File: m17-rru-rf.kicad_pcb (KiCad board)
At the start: 4 copper layers, 255 x 165 mm, 197 parts, among them J1 13.8V, J2 Conn_Coaxial, J3 DBG_CONN, J4 SWD_CONN, J5 DA15_CONN, J6 Conn_Coaxial, Q1 BSS138, Q2 BSS138, Q3 NP100P04PDG, U1 LT1013DIDR, U10 GAT-30+, U11 CC1200, U12 AD8318, U13 AD8318, U14 STM32F405RGT6, U15 WH3538X-1, U2 LM317_SOT-223, U3 TL431, U4 RA60H3847H1, U5 TP6841, U6 TP6841, U7 CC1200, U8 GAT-30+, U9 SYBD-30-62HP+, X1 40MHz, Y1 12MHz

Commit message: TP updates, temp sensor added
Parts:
- added C90: 1u, Capacitor_SMD:C_0603_1608Metric, F.Cu at (124.7, 85.9)
- added C91: 100n, Capacitor_SMD:C_0603_1608Metric, F.Cu at (124.7, 88.4)
- added C92: 1n, Capacitor_SMD:C_0603_1608Metric, F.Cu at (124.7, 91.0)
- added FB8: Bead, Inductor_SMD:L_0603_1608Metric, F.Cu at (124.7, 98.0)
- added FB9: Bead, Inductor_SMD:L_0603_1608Metric, F.Cu at (124.7, 93.5)
- added J7: N_PAD, Connector_Coaxial:SMA_Samtec_SMA-J-P-X-ST-EM1_EdgeMount, F.Cu at (141.0, 81.3)
- added TP14: TP, TestPoint:TestPoint_Pad_D1.5mm, F.Cu at (130.0, 103.0)
- added TP15: TP, TestPoint:TestPoint_Pad_D1.5mm, F.Cu at (124.5, 103.0)
- added TP16: TP, TestPoint:TestPoint_Pad_D1.5mm, F.Cu at (130.5, 86.5)
- added TP17: TP, TestPoint:TestPoint_Pad_D1.5mm, F.Cu at (130.5, 90.0)
- C10, C17: value 100u/50V -> 100n; footprint Capacitor_SMD:CP_Elec_8x10.5 -> Capacitor_SMD:C_0603_1608Metric
- C12: value 100u/50V -> 1u; footprint Capacitor_SMD:CP_Elec_8x10.5 -> Capacitor_SMD:C_0603_1608Metric
- C13, C14: value 100n -> 100u/50V; footprint Capacitor_SMD:C_0603_1608Metric -> Capacitor_SMD:CP_Elec_8x10.5
- C18: value 22u/6.3V -> 100n
- C19: value 22u/6.3V -> 100u/50V; footprint Capacitor_SMD:C_0603_1608Metric -> Capacitor_SMD:CP_Elec_8x10.5
- C20, C21: value 47n -> 22u/6.3V
- C23, C48: value 9p1 -> 47n
- C25: value 1n5 -> 9p1
- C27, C51: value 47n -> 1n5
- C33, C56, C79: value 100n -> 47n
- C35, C82: value 10n -> 100n
- C36: value 220n -> 47n
- C37: value 39p -> 10n
- C38: value 56p -> 220n
- C39: value 2p2 -> 39p
- C40: value 10n -> 56p
- C41: value 5p1 -> 2p2
- C42: value 100p -> 10n
- C43: value 6p2 -> 5p1
- C44: value 47n -> 100p
- C45: value 47n -> 6p2
- C49: value 1n5 -> 47n
- C50: value 47n -> 9p1
- C55, C61: value 5p1 -> 47n
- C57: value 47n -> 5p1
- C58: value 5p1 -> 100n
- C60: value 10n -> 5p1
- C62: value 6p2 -> 10n
- C63: value 220n -> 5p1
- C64: value 1u -> 6p2
- C65: value 100n -> 220n
- C66: value 1n -> 1u
- C69, C72, C89: value 1n -> 100n
- C70: value 100n -> 1n
- C73, C74: value 10p -> 1n
- C75, C76: value 2u2 -> 10p
- C77, C78: value 1u -> 2u2
- C80: value 100n -> 1u
- C81: value 10n -> 1u
- C84, C85: value 100n -> 10n
- C87: value 1u -> 100n
- J1: value 13.8V -> LMT87LPM; footprint TestPoint:TestPoint_Pad_D3.0mm -> Connector_PinHeader_2.54mm:PinHeader_1x03_P2.54mm_Vertical_SMD_Pin1Left
- J2: value Conn_Coaxial -> 13.8V; footprint Connector_Coaxial:SMA_Samtec_SMA-J-P-X-ST-EM1_EdgeMount -> TestPoint:TestPoint_Pad_D3.0mm
- J3: value DBG_CONN -> N_PAD; footprint Connector_PinHeader_2.54mm:PinHeader_1x05_P2.54mm_Vertical_SMD_Pin1Left -> Connector_Coaxial:SMA_Samtec_SMA-J-P-X-ST-EM1_EdgeMount
- J4: value SWD_CONN -> DBG_CONN
- J5: value DA15_CONN -> SWD_CONN; footprint Connector_PinHeader_2.54mm:PinHeader_2x08_P2.54mm_Vertical_SMD -> Connector_PinHeader_2.54mm:PinHeader_1x05_P2.54mm_Vertical_SMD_Pin1Left
- J6: value Conn_Coaxial -> DA15_CONN; footprint Connector_Coaxial:SMA_Samtec_SMA-J-P-X-ST-EM1_EdgeMount -> Connector_PinHeader_2.54mm:PinHeader_2x08_P2.54mm_Vertical_SMD
- moved J1 241.1 mm to (89.5, 202.3)
- moved J3 226.1 mm to (322.5, 64.5), turned to 90 degrees
- moved U8 215.0 mm to (306.9, 81.2), turned to 180 degrees
- moved C87 200.8 mm to (106.0, 153.8)
- moved U6 196.9 mm to (92.7, 191.0)
- moved R21 196.9 mm to (90.0, 184.8)
- moved U14 176.5 mm to (93.7, 102.4)
- moved J2 173.6 mm to (142.0, 102.0)
- moved U13 158.9 mm to (88.3, 183.3)
- moved J6 152.5 mm to (166.8, 161.5)
- moved R22 150.9 mm to (101.4, 198.1)
- moved R40 149.1 mm to (131.2, 200.7)
- moved U7 149.1 mm to (152.9, 193.4)
- moved TP13 129.8 mm to (180.1, 161.5)
- moved C86 129.8 mm to (180.3, 166.6)
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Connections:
- C10 pad 1: /RF PA/RF_PA_VDD -> Net-(J1-Pin_1)
- C11 pad 1: /Power supply/13.8V_OUT -> /RF PA/RF_PA_VDD
- C12 pad 1: /Power supply/13.8V_OUT -> /Exciter/3.3V_IN
- C15 pad 1: Net-(U5-BST) -> /Power supply/13.8V_OUT
- C15 pad 2: Net-(U5-SW) -> GND
- C16 pad 1: Net-(U6-BST) -> /Power supply/13.8V_OUT
- C16 pad 2: Net-(U6-SW) -> GND
- C17 pad 1: /Power supply/13.8V_OUT -> Net-(U5-BST)
- C17 pad 2: GND -> Net-(U5-SW)
- C18 pad 1: GND -> Net-(U6-BST)
- C18 pad 2: /Exciter/3.3V_IN -> Net-(U6-SW)
- C19 pad 1: GND -> /Power supply/13.8V_OUT
- C19 pad 2: /Power supply/5V_OUT -> GND
- C20 pad 1: /Exciter/EXCITER_3V3 -> GND
- C20 pad 2: GND -> /Exciter/3.3V_IN
- C21 pad 1: /Exciter/EXCITER_3V3 -> GND
- C21 pad 2: GND -> /Power supply/5V_OUT
- C23 pad 1: /Exciter/40M_OUT -> /Exciter/EXCITER_3V3
- C23 pad 2: Net-(U7-EXT_XOSC) -> GND
- C25 pad 1: Net-(U7-LPF0) -> /Exciter/40M_OUT
- C25 pad 2: Net-(U7-LPF1) -> Net-(U7-EXT_XOSC)
- C27 pad 1: /Exciter/EXCITER_3V3 -> Net-(U7-LPF0)
- C27 pad 2: GND -> Net-(U7-LPF1)
- C32 pad 1: Net-(U7-DCPL_XOSC) -> /Exciter/EXCITER_3V3
- C33 pad 1: /Exciter/3.3V_IN -> /Exciter/EXCITER_3V3
- C34 pad 1: Net-(U7-DCPL_PFD_CHP) -> Net-(U7-DCPL_XOSC)
- C35 pad 1: Net-(U7-DCPL_VCO) -> /Exciter/3.3V_IN
- C36 pad 1: Net-(U7-DCPL) -> Net-(U7-DCPL_PFD_CHP)
- C37 pad 1: Net-(C37-Pad1) -> Net-(U7-DCPL_VCO)
- C37 pad 2: Net-(U7-PA) -> GND
- C38 pad 1: /Exciter/EXCITER_3V3 -> Net-(U7-DCPL)
- C38 pad 2: Net-(C38-Pad2) -> GND
- C39 pad 2: Net-(C37-Pad1) -> Net-(U7-PA)
- C40 pad 2: GND -> Net-(C40-Pad2)
- C41 pad 1: Net-(C39-Pad1) -> Net-(C41-Pad1)
- C41 pad 2: GND -> Net-(C39-Pad1)
- C43 pad 1: Net-(C43-Pad1) -> Net-(C41-Pad1)
- C44 pad 1: /Receiver/RX_3V3 -> /Exciter/EXCITER_3V3
- C45 pad 1: /Receiver/RX_3V3 -> Net-(C45-Pad1)
- C48 pad 1: Net-(U11-EXT_XOSC) -> /Receiver/RX_3V3
- C48 pad 2: /Exciter/40M_OUT -> GND
- C49 pad 1: Net-(U11-LPF0) -> /Receiver/RX_3V3
- C49 pad 2: Net-(U11-LPF1) -> GND
- C50 pad 1: /Receiver/RX_3V3 -> Net-(U11-EXT_XOSC)
- C50 pad 2: GND -> /Exciter/40M_OUT
- C51 pad 1: /Receiver/RX_3V3 -> Net-(U11-LPF0)
- C51 pad 2: GND -> Net-(U11-LPF1)
- C55 pad 1: Net-(U11-LNA_P) -> /Receiver/RX_3V3
- C55 pad 2: Net-(C55-Pad2) -> GND
- C56 pad 1: /Exciter/3.3V_IN -> /Receiver/RX_3V3
- C57 pad 1: Net-(U11-DCPL_XOSC) -> Net-(U11-LNA_P)
- C57 pad 2: GND -> Net-(C57-Pad2)
- C58 pad 1: Net-(U11-LNA_N) -> /Exciter/3.3V_IN
- C59 pad 1: Net-(U11-DCPL_PFD_CHP) -> Net-(U11-DCPL_XOSC)
- C60 pad 1: Net-(U11-DCPL_VCO) -> Net-(U11-LNA_N)
- C61 pad 1: Net-(C61-Pad1) -> Net-(U11-DCPL_PFD_CHP)
- C61 pad 2: Net-(C61-Pad2) -> GND
- C62 pad 1: Net-(C61-Pad2) -> Net-(U11-DCPL_VCO)
- C63 pad 1: Net-(U11-DCPL) -> Net-(C63-Pad1)
- C63 pad 2: GND -> Net-(C63-Pad2)
- C64 pad 1: /Power supply/5V_OUT -> Net-(C63-Pad2)
- C65 pad 1: Net-(U12-CLPF) -> Net-(U11-DCPL)
- C66 pad 1: GND -> /Power supply/5V_OUT
- C66 pad 2: Net-(U12-INLO) -> GND
- C67 pad 1: /RF detectors/RF_DET_5V -> Net-(U12-CLPF)
- C68 pad 1: /RF coupler/FWD_RF -> GND
- C68 pad 2: Net-(U12-INHI) -> Net-(U12-INLO)
- C70 pad 1: Net-(U13-CLPF) -> /RF coupler/FWD_RF
- C70 pad 2: GND -> Net-(U12-INHI)
- C71 pad 1: GND -> /RF detectors/RF_DET_5V
- C71 pad 2: Net-(U13-INLO) -> GND
- C72 pad 1: /RF coupler/REF_RF -> Net-(U13-CLPF)
- C72 pad 2: Net-(U13-INHI) -> GND
- C73 pad 1: /MCU/OSC1 -> GND
- C73 pad 2: GND -> Net-(U13-INLO)
- C74 pad 1: /MCU/OSC2 -> /RF coupler/REF_RF
- C74 pad 2: GND -> Net-(U13-INHI)
- C75 pad 1: Net-(U14-VCAP_1) -> /MCU/OSC1
- C76 pad 1: Net-(U14-VCAP_2) -> /MCU/OSC2
- C77 pad 1: /Exciter/3.3V_IN -> Net-(U14-VCAP_1)
- C78 pad 1: /Exciter/3.3V_IN -> Net-(U14-VCAP_2)
- C79 pad 1: /MCU/MCU_3V3 -> Net-(U14-PA2)
- C80 pad 1: /MCU/MCU_VDDA_3V3 -> /Exciter/3.3V_IN
- C81 pad 1: /MCU/MCU_3V3 -> /Exciter/3.3V_IN
- C82 pad 1: /MCU/MCU_VDDA_3V3 -> /MCU/MCU_3V3
- C83 pad 1: /MCU/MCU_3V3 -> /MCU/MCU_VDDA_3V3
- C85 pad 1: /MCU/MCU_3V3 -> /MCU/MCU_VDDA_3V3
- C87 pad 1: /Exciter/3.3V_IN -> /MCU/MCU_3V3
- C88 pad 1: /Interface/INTERFACE_3V3 -> /MCU/MCU_3V3
- C89 pad 1: /Interface/INTERFACE_3V3 -> /MCU/MCU_3V3
- FB2 pad 1: /Exciter/EXCITER_3V3 -> /Exciter/3.3V_IN
- FB2 pad 2: /Exciter/3.3V_IN -> Net-(J1-Pin_1)
- FB3 pad 1: /Receiver/RX_3V3 -> /Exciter/EXCITER_3V3
- FB4 pad 1: /Power supply/5V_OUT -> /Receiver/RX_3V3
- FB4 pad 2: /RF detectors/RF_DET_5V -> /Exciter/3.3V_IN
- FB5 pad 1: /Exciter/3.3V_IN -> /Power supply/5V_OUT
- FB5 pad 2: /MCU/MCU_3V3 -> /RF detectors/RF_DET_5V
- FB6 pad 1: /Exciter/3.3V_IN -> Net-(U14-PA2)
- FB6 pad 2: /MCU/MCU_VDDA_3V3 -> /Interface/TEMP_SENSE
- FB7 pad 2: /Interface/INTERFACE_3V3 -> /MCU/MCU_3V3
- J1 pad 1: /Power supply/13.8V_OUT -> Net-(J1-Pin_1)
- J2 pad 1: Net-(J2-In) -> /Power supply/13.8V_OUT
- J3 pad 1: /MCU/TP1 -> Net-(J3-In)
- J3 pad 2: /MCU/TP2 -> GND
- J4 pad 1: GND -> /MCU/TP1
- J4 pad 2: /nRST -> /MCU/TP2
- J4 pad 3: /MCU/SWDIO -> /MCU/DBG_TX
- J4 pad 4: /MCU/SWDCLK -> /MCU/DBG_RX
- J4 pad 5: /MCU/MCU_3V3 -> GND
- J5 pad 1: /nRST -> GND
- J5 pad 2: /SPI_MISO -> /nRST
- J5 pad 3: /SPI_MOSI -> /MCU/SWDIO
- J5 pad 4: /SPI_SCK -> /MCU/SWDCLK
- J5 pad 5: /TX_nCS -> /MCU/MCU_3V3
- J6 pad 1: /RF input filter/RF_OUT -> /nRST
- J6 pad 2: GND -> /SPI_MISO
- L10 pad 1: Net-(C61-Pad1) -> Net-(C63-Pad1)
- L10 pad 2: Net-(C55-Pad2) -> Net-(C57-Pad2)
- L11 pad 2: Net-(C61-Pad2) -> Net-(C63-Pad2)
- L3 pad 1: Net-(C38-Pad2) -> Net-(C40-Pad2)
- L4 pad 1: Net-(C39-Pad1) -> Net-(C41-Pad1)
- L4 pad 2: Net-(C37-Pad1) -> Net-(C39-Pad1)
- L5 pad 1: Net-(C43-Pad1) -> Net-(C45-Pad1)
- L5 pad 2: Net-(C39-Pad1) -> Net-(C41-Pad1)
- L6 pad 2: Net-(C43-Pad1) -> Net-(C45-Pad1)
- L9 pad 2: Net-(C55-Pad2) -> Net-(C57-Pad2)
- R31 pad 1: Net-(C38-Pad2) -> Net-(C40-Pad2)
- U14 pad 16: /MCU/AIN2 -> Net-(U14-PA2)
- U9 pad 1: Net-(J2-In) -> Net-(J3-In)
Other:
- board size 255 x 165 mm -> 250 x 160 mm

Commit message: started pcb layout
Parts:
- moved U13 235.3 mm to (306.0, 94.0)
- moved R37 193.3 mm to (298.0, 93.5), turned to 90 degrees
- moved R39 179.8 mm to (310.5, 93.5), turned to 90 degrees
- moved R38 177.6 mm to (306.0, 86.0)
- moved TP17 177.2 mm to (307.5, 98.5)
- moved U12 170.1 mm to (293.5, 94.0)
- moved TP16 165.0 mm to (295.0, 98.5)
- moved C73 158.6 mm to (305.0, 89.0), turned to -90 degrees
- moved C72 154.1 mm to (305.0, 98.5), turned to -90 degrees
- moved C74 153.8 mm to (307.0, 89.0), turned to -90 degrees
- moved C71 148.0 mm to (301.0, 103.0), turned to -90 degrees
- moved C70 145.9 mm to (294.5, 89.0), turned to -90 degrees
- moved C66 141.9 mm to (322.0, 104.0)
- moved R36 120.9 mm to (293.5, 86.0)
- moved FB5 120.8 mm to (314.0, 109.5), turned to 90 degrees
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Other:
- outline, holes or cut-outs redrawn

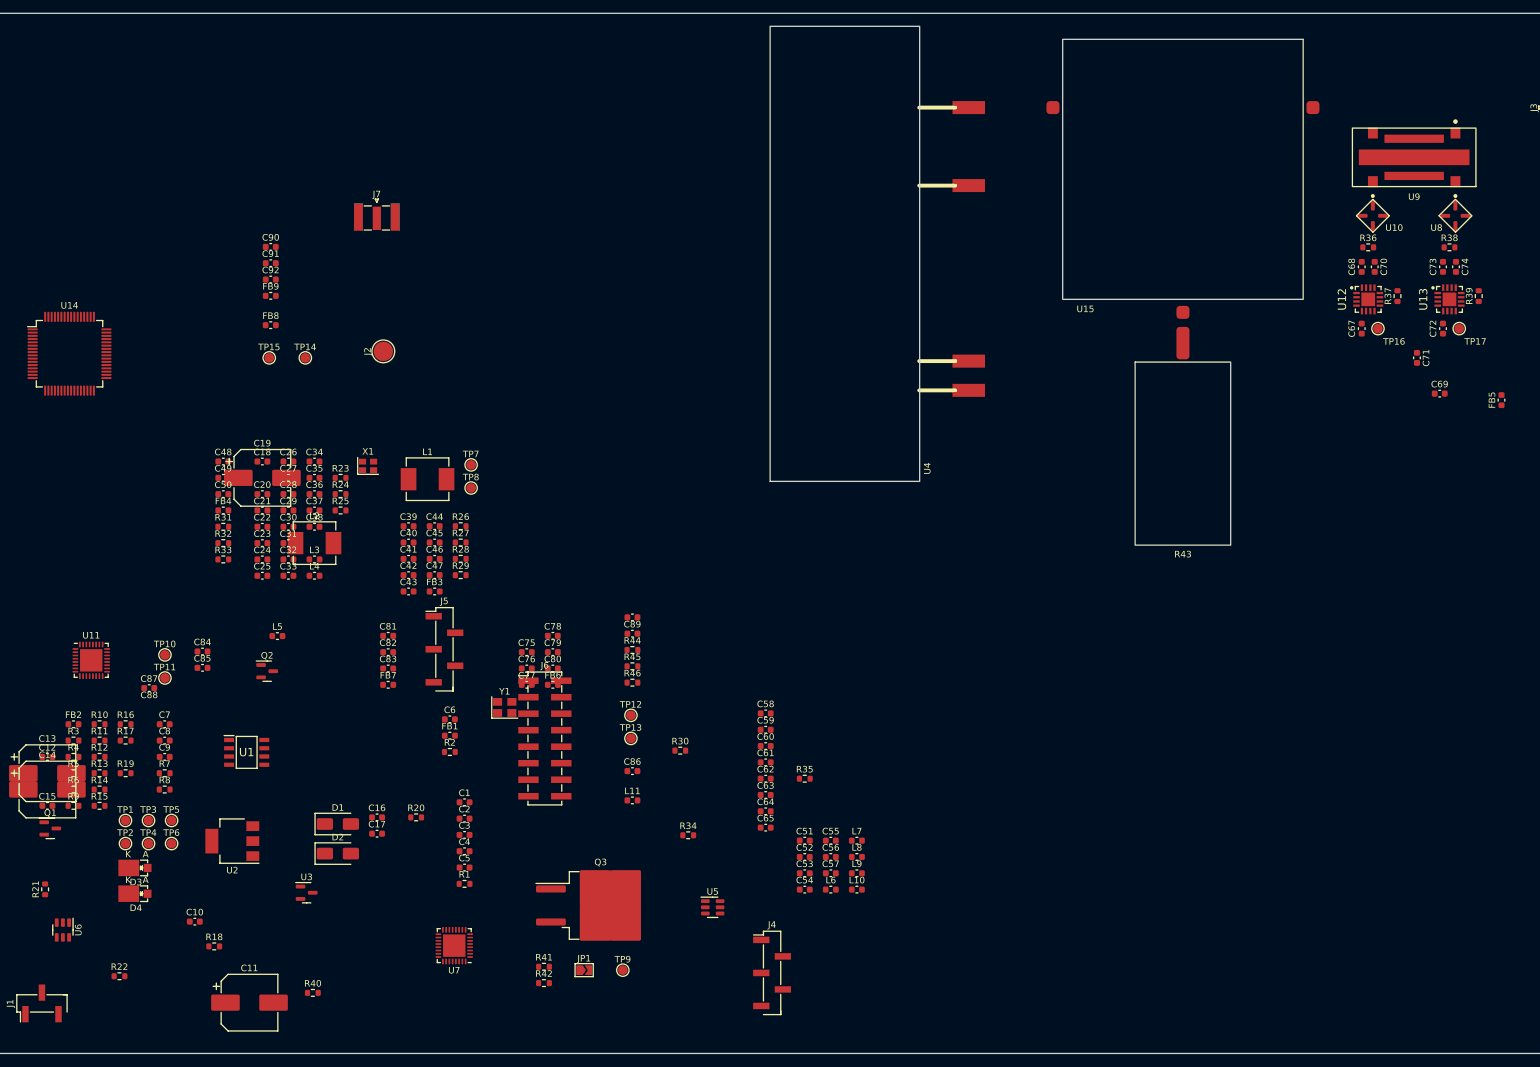
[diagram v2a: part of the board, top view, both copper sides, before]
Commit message: moved around a few components
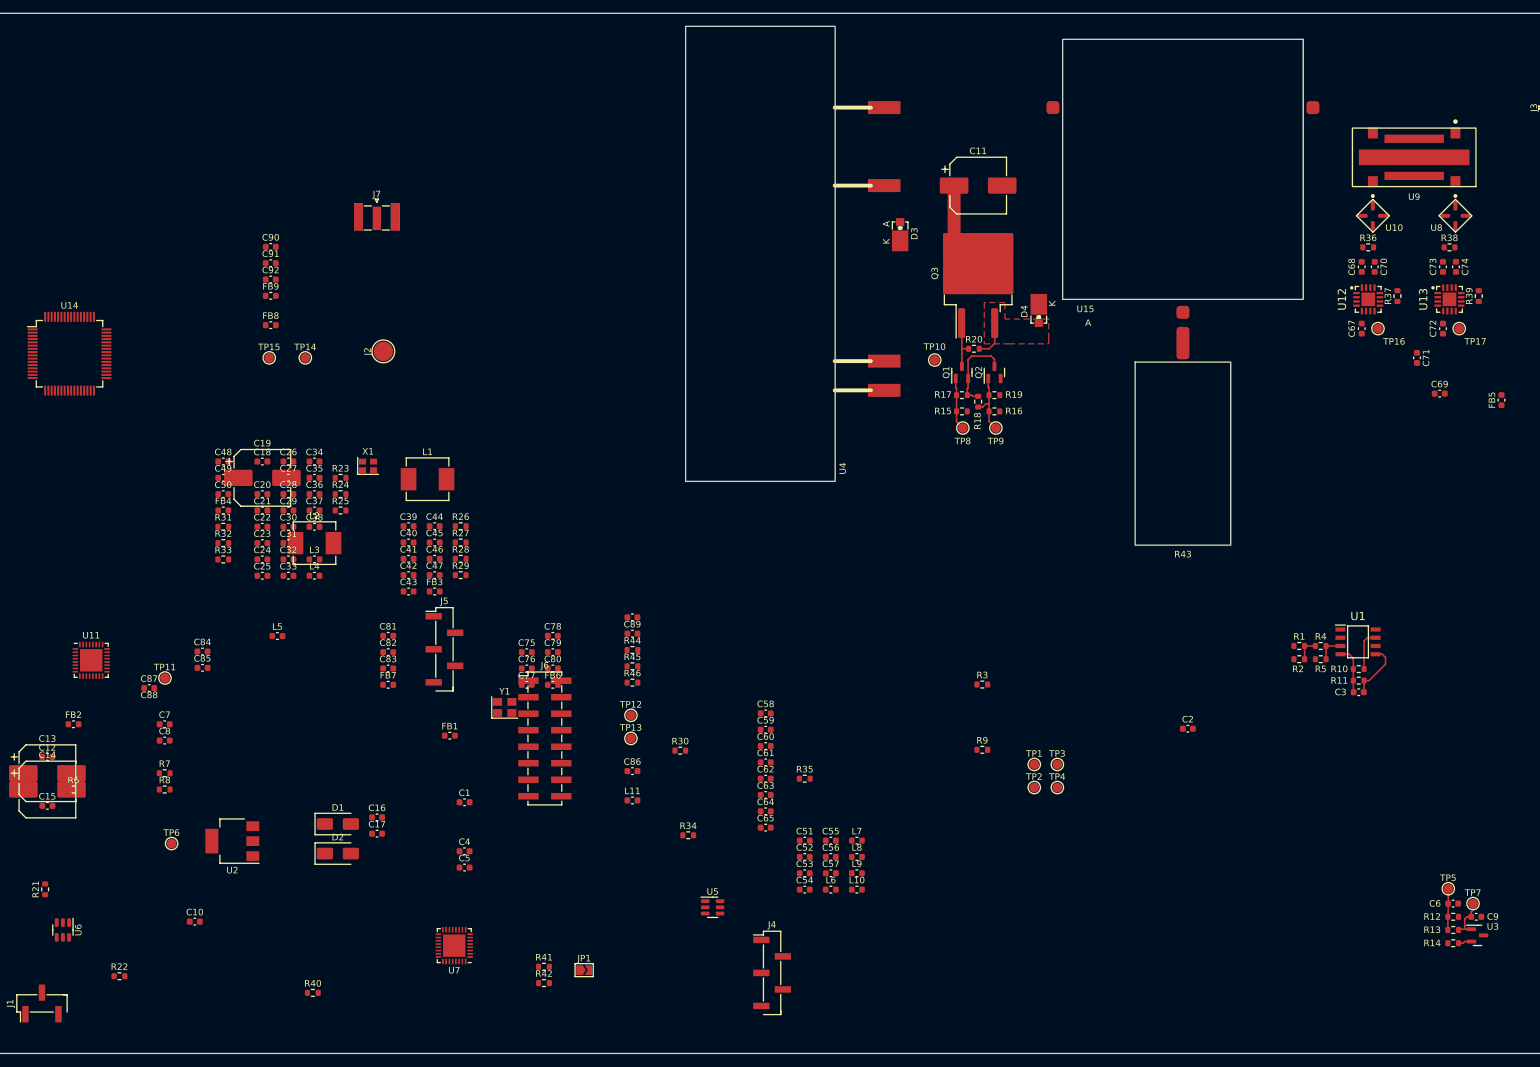
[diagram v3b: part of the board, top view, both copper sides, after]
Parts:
- moved R12 209.7 mm to (306.6, 189.0), turned to 180 degrees
- moved R13 209.6 mm to (306.6, 191.0), turned to 180 degrees
- moved R14 209.6 mm to (306.6, 193.0), turned to 180 degrees
- moved C9 203.2 mm to (310.1, 189.0), turned to 180 degrees
- moved TP5 196.7 mm to (305.8, 184.7)
- moved R11 193.9 mm to (292.0, 152.7)
- moved R10 193.9 mm to (292.0, 150.9)
- moved R5 192.7 mm to (286.2, 149.4)
- moved R4 192.6 mm to (286.2, 147.3)
- moved U3 180.2 mm to (310.3, 191.8)
- moved U1 171.8 mm to (291.9, 146.7)
- moved C11 168.4 mm to (233.5, 76.5)
- moved TP7 168.2 mm to (309.6, 186.9)
- moved D4 165.4 mm to (242.8, 95.8), turned to -90 degrees
- moved C6 156.9 mm to (306.6, 186.9)
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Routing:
- net /RF PA/RF_PA_VDD: track 0.00 -> 13.5 mm
- net Net-(Q1-S): track 0.00 -> 12.8 mm
- net Net-(Q2-G): track 0.00 -> 9.98 mm
- net Net-(U3-K): track 0.00 -> 8.93 mm
- net /RF PA/RF_PA_VGG: track 0.00 -> 8.90 mm
- net Net-(Q1-G): track 0.00 -> 8.07 mm
- net Net-(U1-2IN-): track 0.00 -> 7.48 mm
- net /RF PA/RF_PA_1V1: track 0.00 -> 6.38 mm
- net Net-(U1-1OUT): track 0.00 -> 6.31 mm
- net Net-(Q1-D): track 0.00 -> 5.96 mm
- net /Power supply/13.8V_OUT: track 0.00 -> 5.82 mm
- net Net-(U1-2IN+): track 0.00 -> 4.23 mm
- net Net-(R1-Pad2): track 0.00 -> 3.68 mm
- added copper zone on F.Cu, net /Power supply/13.8V_OUT

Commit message: pcb update
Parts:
- moved R6 224.6 mm to (313.0, 117.9)
- moved R7 207.0 mm to (309.4, 117.9)
- moved R8 204.1 mm to (305.9, 117.9)
- moved U2 196.1 mm to (307.2, 122.9)
- moved TP6 193.9 mm to (294.8, 120.7)
- moved C8 193.7 mm to (298.0, 122.4)
- moved C78 193.1 mm to (-11.1, 217.9)
- moved C79 193.1 mm to (-11.1, 220.4)
- moved C80 193.1 mm to (-11.1, 222.9)
- moved FB6 193.1 mm to (-11.1, 225.4)
- moved C75 193.1 mm to (-15.1, 220.4)
- moved C76 193.1 mm to (-15.1, 222.9)
- moved C77 193.1 mm to (-15.1, 225.4)
- moved R41 193.1 mm to (-12.4, 268.8)
- moved R42 193.1 mm to (-12.4, 271.3)
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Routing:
- net /Exciter/EXCITER_3V3: track 0.00 -> 87.9 mm, vias 0 -> 7
- net /RF detectors/RF_DET_5V: track 0.00 -> 50.0 mm, vias 0 -> 4
- net /RF PA/RF_PA_7V: track 0.00 -> 26.1 mm, vias 0 -> 2
- net Net-(D2-A): track 0.00 -> 23.2 mm
- net Net-(D1-A): track 0.00 -> 22.5 mm
- net /Power supply/13.8V_OUT: track 5.82 -> 19.7 mm, vias 0 -> 1
- net /RF PA/RF_PA_VDD: track 13.5 -> 24.1 mm
- net Net-(J3-In): track 0.00 -> 9.32 mm
- net Net-(U1-1IN-): track 0.00 -> 9.10 mm
- net Net-(U7-PA): track 0.00 -> 8.89 mm
- net Net-(U1-1OUT): track 6.31 -> 14.5 mm
- net /Circulator/RF_OUT: track 0.00 -> 7.98 mm
- net /FWD_SENSE: track 0.00 -> 7.11 mm
- net /Exciter/40M_OUT: track 0.00 -> 6.59 mm
- net Net-(J1-Pin_1): track 0.00 -> 6.16 mm
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- removed copper zone on F.Cu, net /Power supply/13.8V_OUT
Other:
- board size 250 x 160 mm -> 240 x 165 mm

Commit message: pcb update
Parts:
- added REF**: KiCad-Logo2_8mm_SilkScreen, Symbol:KiCad-Logo2_8mm_SilkScreen, F.Cu at (219.0, 56.0)
- added REF**: OSHW-Logo_11.4x12mm_SilkScreen, Symbol:OSHW-Logo_11.4x12mm_SilkScreen, F.Cu at (235.0, 155.0)
- moved J7 286.4 mm to (310.0, 155.0), turned to 90 degrees
- moved U11 283.7 mm to (237.4, 122.4)
- moved JP1 278.8 mm to (238.5, 135.9)
- moved C49 261.0 mm to (244.6, 121.7)
- moved C48 258.7 mm to (240.5, 115.1), turned to 90 degrees
- moved C50 253.6 mm to (232.9, 115.1), turned to 90 degrees
- moved R33 251.2 mm to (229.9, 124.2), turned to 180 degrees
- moved R32 249.5 mm to (229.9, 125.7), turned to 180 degrees
- moved FB4 245.9 mm to (229.9, 130.3), turned to 180 degrees
- moved TP15 235.7 mm to (229.6, 116.3)
- moved C46 232.9 mm to (237.5, 115.1), turned to 90 degrees
- moved C47 232.7 mm to (236.0, 115.1), turned to 90 degrees
- moved L11 221.5 mm to (245.1, 136.9), turned to 90 degrees
- moved C51 214.5 mm to (242.8, 119.4), turned to 180 degrees
- moved R34 212.2 mm to (229.9, 127.3), turned to 180 degrees
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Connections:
- net Net-(J3-In) renamed /RF coupler/RF_OUT_CONN
- net Net-(R43-In) renamed /Circulator/ISOLATED
- net Net-(U10-In) renamed /RF coupler/CPL_FWD
- net Net-(U8-In) renamed /RF coupler/CPL_REF
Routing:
- net /Receiver/RX_3V3: track 0.00 -> 79.7 mm, vias 0 -> 9
- net /RF input filter/RF_OUT: track 0.00 -> 79.1 mm
- net /Circulator/RF_IN: track 0.00 -> 43.9 mm
- net /nRST: track 1.57 -> 16.0 mm, vias 1 -> 3
- net Net-(JP1-B): track 0.00 -> 13.6 mm, vias 0 -> 2
- net /RX_nCS: track 0.00 -> 12.0 mm, vias 0 -> 2
- net /Exciter/RF_OUT: track 0.00 -> 10.2 mm
- net /SPI_MOSI: track 0.00 -> 9.92 mm, vias 0 -> 1
- net /Exciter/3.3V_IN: track 5.38 -> 13.9 mm, vias 1 -> 3
- net Net-(U11-LNA_N): track 0.00 -> 8.29 mm
- net /SPI_SCK: track 0.00 -> 7.57 mm, vias 0 -> 1
- net /FWD_SENSE: track 7.11 -> 14.6 mm, vias 0 -> 2
- net Net-(U11-LNA_P): track 0.00 -> 6.81 mm
- net /Exciter/40M_OUT: track 6.59 -> 13.3 mm, vias 0 -> 1
- net Net-(U11-SO(GPIO1)): track 0.00 -> 6.32 mm
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- added copper zone on F.Cu, net /Power supply/13.8V_OUT
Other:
- board size 240 x 165 mm -> 240 x 125 mm
- board text added: "DUMMY LOAD"
- board text added: "RF IN"
- board text added: "RF OUT"
